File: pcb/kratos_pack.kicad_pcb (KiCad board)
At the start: 4 copper layers, 44.2 x 20.2 mm, 121 parts, among them J1 USB_C_Receptacle_USB2.0, J2 PROG_CONN, J3 DBG_UART, J4 BAT_MID+NTC, J5 BAT_7.4V, J6 BAT_0V, J7 OUT+, J8 OUT-, Q1 AON7403, Q2 AON7414, Q3 AON7414, Q4 UT6MA2TCR, Q5 UT6MA2TCR, Q6 UT6MA2TCR, Q7 DMN2300UFD-7, SW1 WAKEUP, SW2 BOOT, SW3 RST_BTN, U10 24LC32, U11 MIC94300, U12 74LVC2G14, U13 MIC94300, U2 CP2102N-Axx-xQFN20, U3 STM32G071Gx, U4 KTD2026BEWE, U5 BQ25887, U6 BD48xxFVE, U7 INA199, U8 LTC4231, U9 LDK715M33R

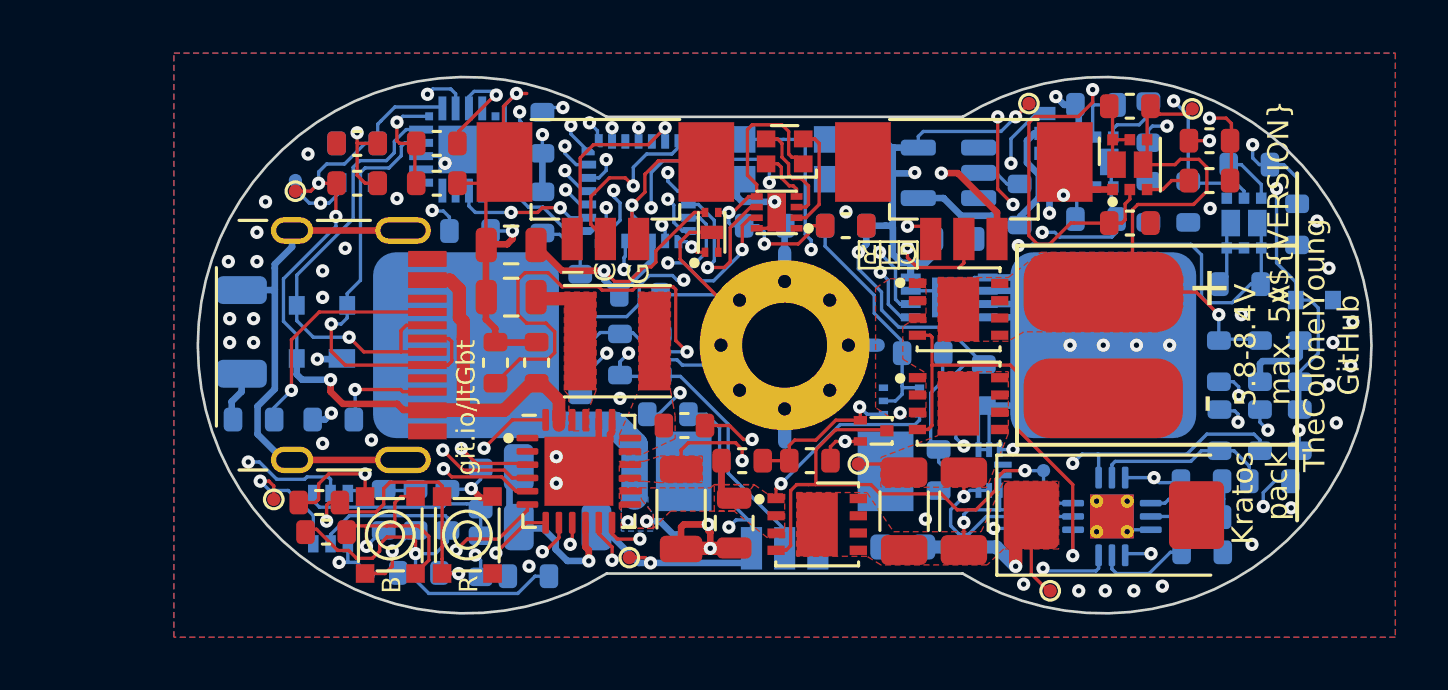
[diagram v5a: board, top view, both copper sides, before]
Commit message: PCB: layout optimization (around LTC4231 and center mounting hole to GND)
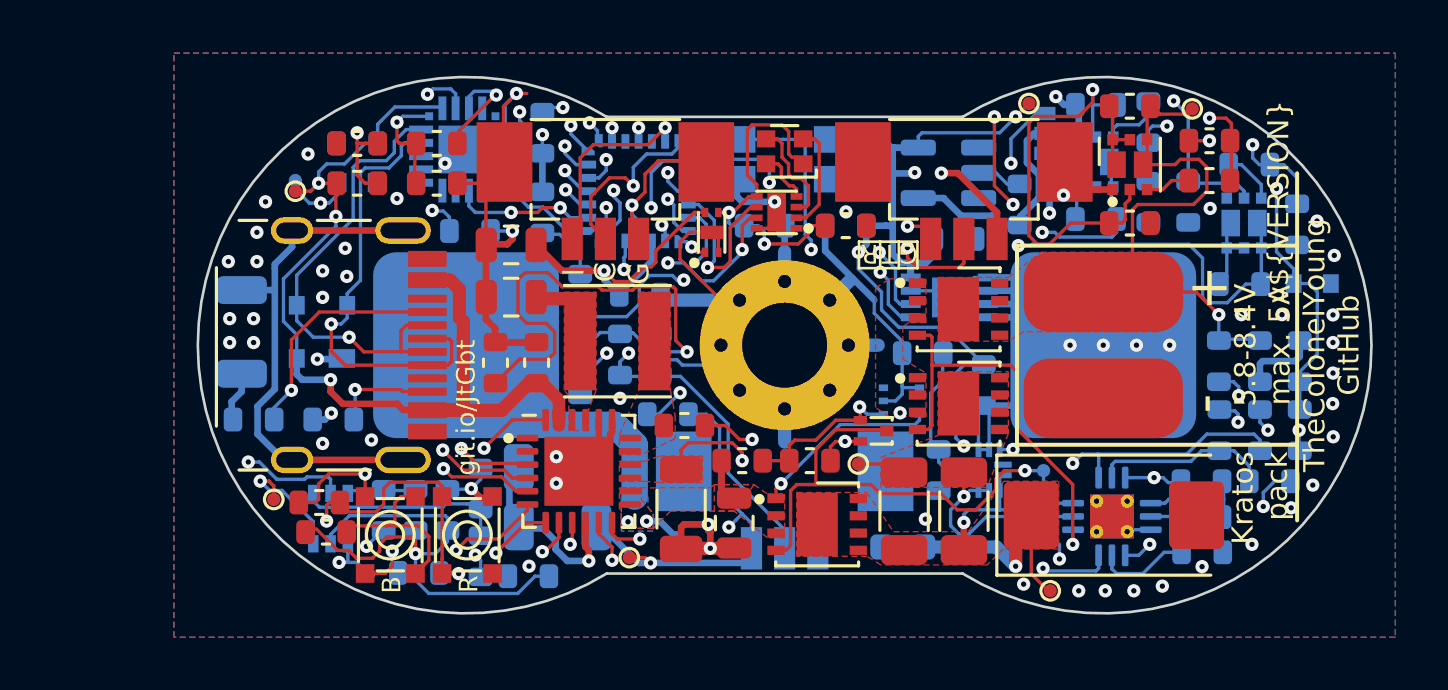
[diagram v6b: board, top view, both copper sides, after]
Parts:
- moved D4 0.63 mm to (170.9, 97.7)
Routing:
- net GND: track 166.2 -> 172.1 mm, vias 59 -> 63
- net /VBAT: track 66.8 -> 69.2 mm
- net Net-(Q2-Pad4): track 16.6 -> 15.7 mm
- net VCC: track 47.7 -> 47.0 mm
- net +3V3: track 117.1 -> 116.5 mm
